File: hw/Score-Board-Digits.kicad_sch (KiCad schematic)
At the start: 65 parts, among them J11 Conn_02x09_Odd_Even, J12 Conn_02x09_Odd_Even, J13 Conn_02x09_Odd_Even

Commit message: Separate Main and Digits projects
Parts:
- DIG1, DIG2: footprint Display_7Segment:SA15-11xxx -> AES_Library:DISP-40101BCR-AES
- DIG5, DIG6: footprint Display_7Segment:SA15-11xxx -> AES_Library:DISP-CL18011BS-AES
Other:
- title: Portable Score Board w/Remote -> Portable Score Board - Digits

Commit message: Digits schmatic ready for layout
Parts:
- removed DIG1, DIG2: WJLEDS40012TUR11, AES_Library:DISP-40101BCR-AES, symbol AES_Library:WJ-LEDS40012TUR11
- removed DIG5 (x3), DIG6: WJLEDS18012TUR11, AES_Library:DISP-CL18011BS-AES, symbol AES_Library:WJ-LEDS18012TUR11
- removed H1 (x2), H2 (x2), H3 (x2), H4 (x2): MountingHole, MountingHole:MountingHole_3.2mm_M3, symbol Mechanical:MountingHole
- removed J12, J13: Conn_02x09_Odd_Even, Connector_PinHeader_2.54mm:PinHeader_2x09_P2.54mm_Vertical, symbol Connector_Generic:Conn_02x09_Odd_Even
- removed LED4: IND-B1, LED_THT:LED_D5.0mm-3, symbol Device:LED
- removed LED5: IND-B2, LED_THT:LED_D5.0mm-3, symbol Device:LED
- removed LED6: IND-B3, LED_THT:LED_D5.0mm-3, symbol Device:LED
- removed LED7: IND-B4, LED_THT:LED_D5.0mm-3, symbol Device:LED
- removed R25, R26, R27, R28, R29, R30, R31: 150, Resistor_THT:R_Axial_DIN0207_L6.3mm_D2.5mm_P10.16mm_Horizontal, symbol Device:R_Small_US
- removed R25, R26, R27, R28, R29, R30, R31, R32 (x2): 0, Resistor_THT:R_Axial_DIN0207_L6.3mm_D2.5mm_P10.16mm_Horizontal, symbol Device:R_Small_US
- added Opt1, Opt2, Opt3, Opt4, Opt5: Opt_1-2, Connector_PinHeader_2.54mm:PinHeader_1x03_P2.54mm_Vertical, symbol AES_Library:Opt_1_of_2
- DIG1: renamed from DIG5; footprint AES_Library:DISP-CL18011BS-AES -> Connector_PinHeader_2.54mm:PinHeader_1x03_P2.54mm_Vertical
- renumbered DIG5 to DIG2, DIG1 to DIG3, DIG2 to DIG4, J11 to J1, LED4 to LED1, LED5 to LED2, LED6 to LED3, LED7 to LED4, R25 to R1, R22 to R10, R23 to R11, R24 to R12, R21 to R13, R22 to R14, R23 to R15, R24 to R16, R26 to R2, R27 to R3, R28 to R4, R29 to R5, R30 to R6, R31 to R7, R32 to R8, R21 to R9
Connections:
- net SD.B.E is gone; now on net SD.E: R13.1
- net SD.B.F is gone; now on net SD.F: R14.1
- net SD.B.G is gone; now on net SD.G: R15.1
- net SD.B.P is gone; now on net SD.P: R16.1
- net at DIG2.1 (CA), DIG2.5 (CA), DIG4.1 (CA)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: now also Opt3.2 (Pin_Common), Opt4.2 (Pin_Common); no longer J1.4 (Pin_4)
- net at R13.2: now also LED1.1 (K), R9.2
- net at R16.2: now also LED4.1 (K), R12.2
- net at LED3.1 (K), R11.2: now also R15.2
- net at DIG1.1 (CA), DIG1.5 (CA), DIG3.1 (CA)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: now also Opt1.2 (Pin_Common), Opt2.2 (Pin_Common); no longer J1.2 (Pin_2)
- net at R14.2: now also LED2.1 (K), R10.2
- net at LED1.2 (A), LED2.2 (A), LED3.2 (A)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: now also Opt5.2 (Pin_Common); no longer J1.14 (Pin_14)
- net at J1.10 (Pin_10): now also Opt2.1 (Pin_A)
- net at J1.12 (Pin_12): now also Opt4.1 (Pin_A)
- net at J1.16 (Pin_16): now also Opt5.3 (Pin_B)
- net at J1.6 (Pin_6): now also Opt1.3 (Pin_B)
- net at J1.8 (Pin_8): now also Opt3.3 (Pin_B)
- net SD.A.A renamed SD.A
- net SD.A.B renamed SD.B
- net SD.A.C renamed SD.C
- net SD.A.D renamed SD.D
- net SD.A.E renamed SD.E
- net SD.A.F renamed SD.F
- net SD.A.G renamed SD.G
- net SD.A.P renamed SD.P
- new net: J1.4 (Pin_4), Opt3.1 (Pin_A)
- new net: J1.2 (Pin_2), Opt1.1 (Pin_A)
- new net: J1.14 (Pin_14), Opt5.1 (Pin_A)
- no-connect marks 16 -> 2
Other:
- note added: "(LARGE DIGIT ASSY)"
- note added: "(SMALL DIGIT ASSY)"
- note added: "Indicators A/B/None Populate Resistors for A-D or E-P and select Option A or B"
- note removed: "(LARGE DIGIT OPTION)"
- note removed: "(SMALLER DIGIT OPTION)"
- note removed: "PERIOD / TIME (BOARD C)"
- note removed: "TEAM A SCORE & INDICATORS (BOARD A)"
- note removed: "TEAM B SCORE & INDICATORS (BOARD B)"
- moved on the sheet: DIG1, DIG2, DIG3, DIG4, H1, H2, H3, H4, J1, LED1, LED2, LED3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

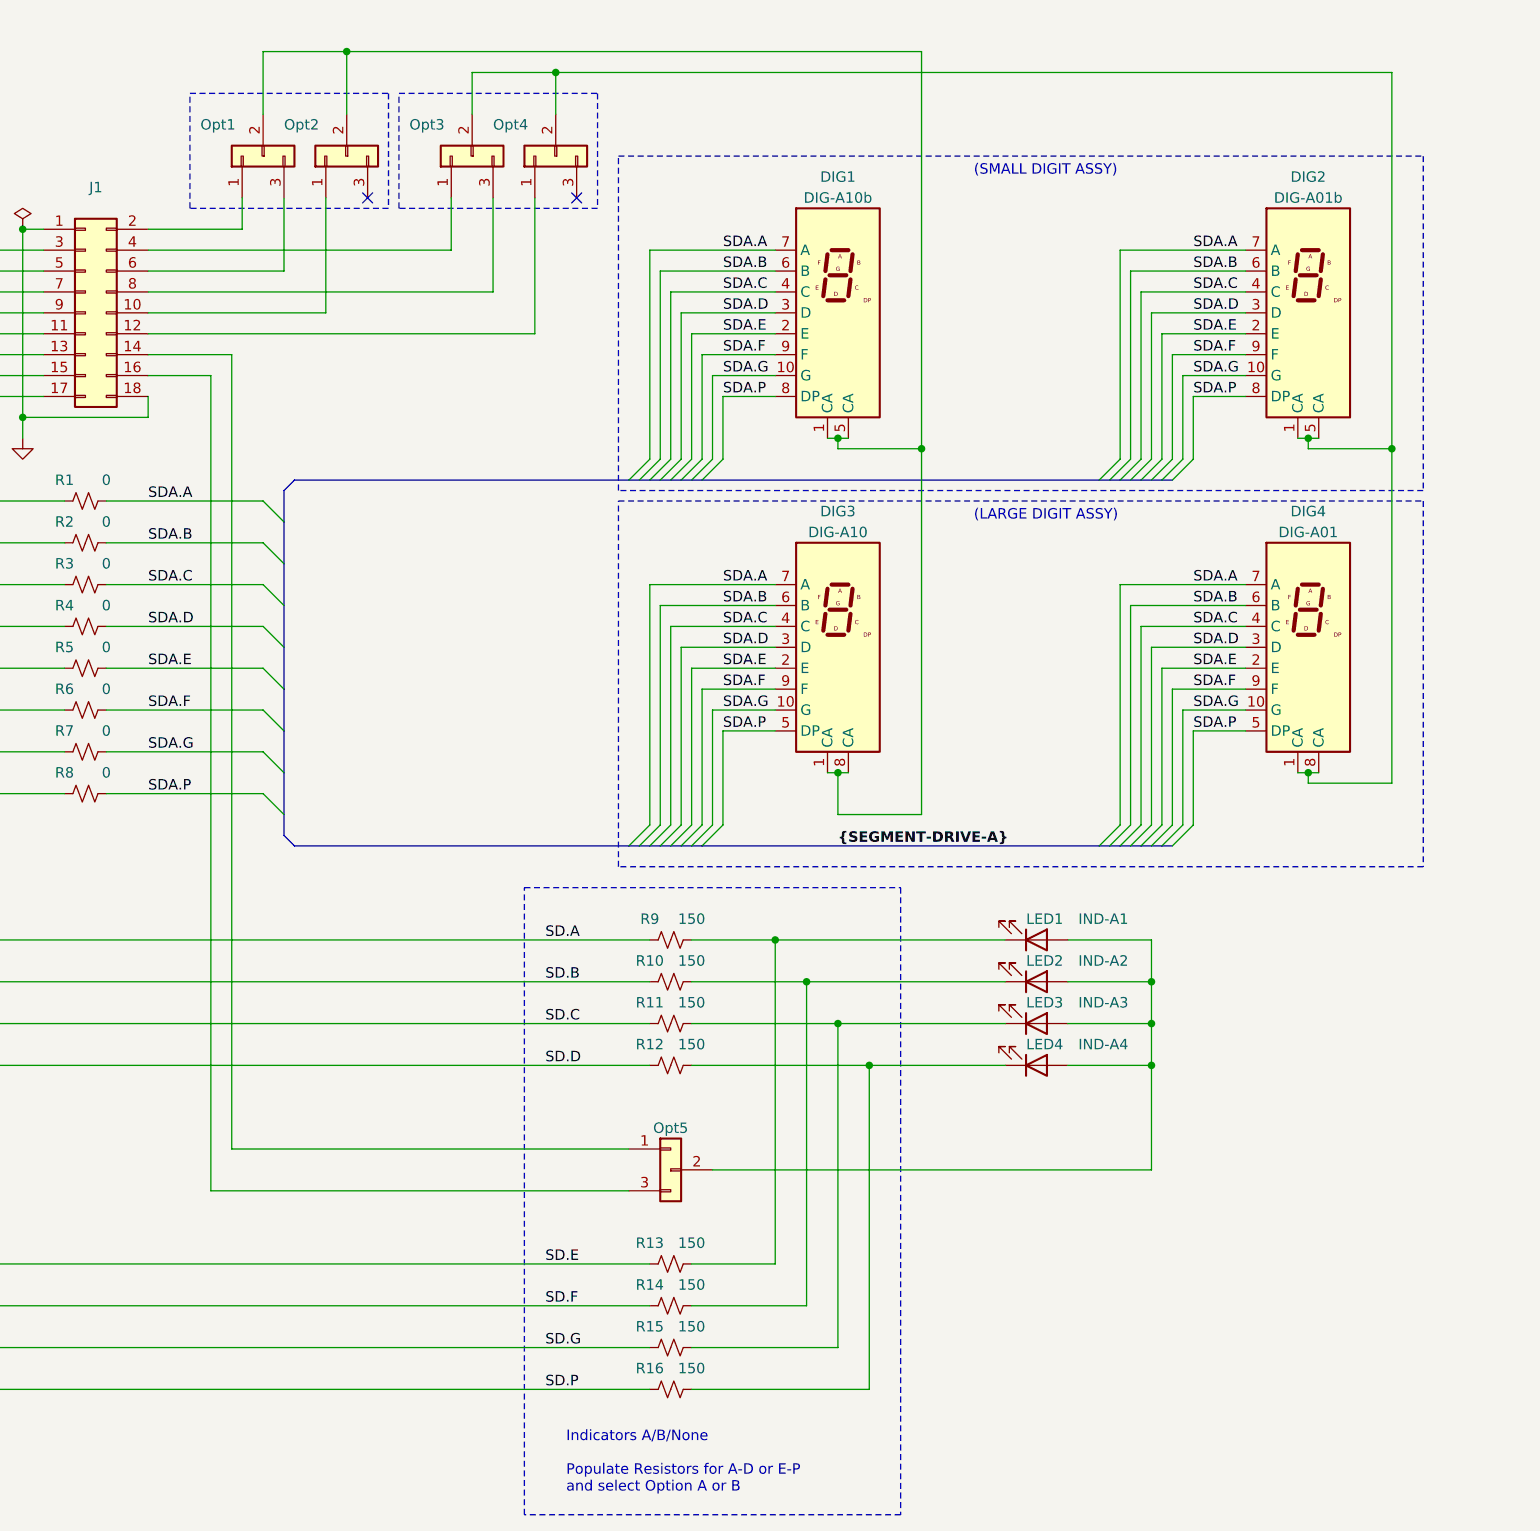
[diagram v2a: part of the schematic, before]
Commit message: Initial PCB component placement
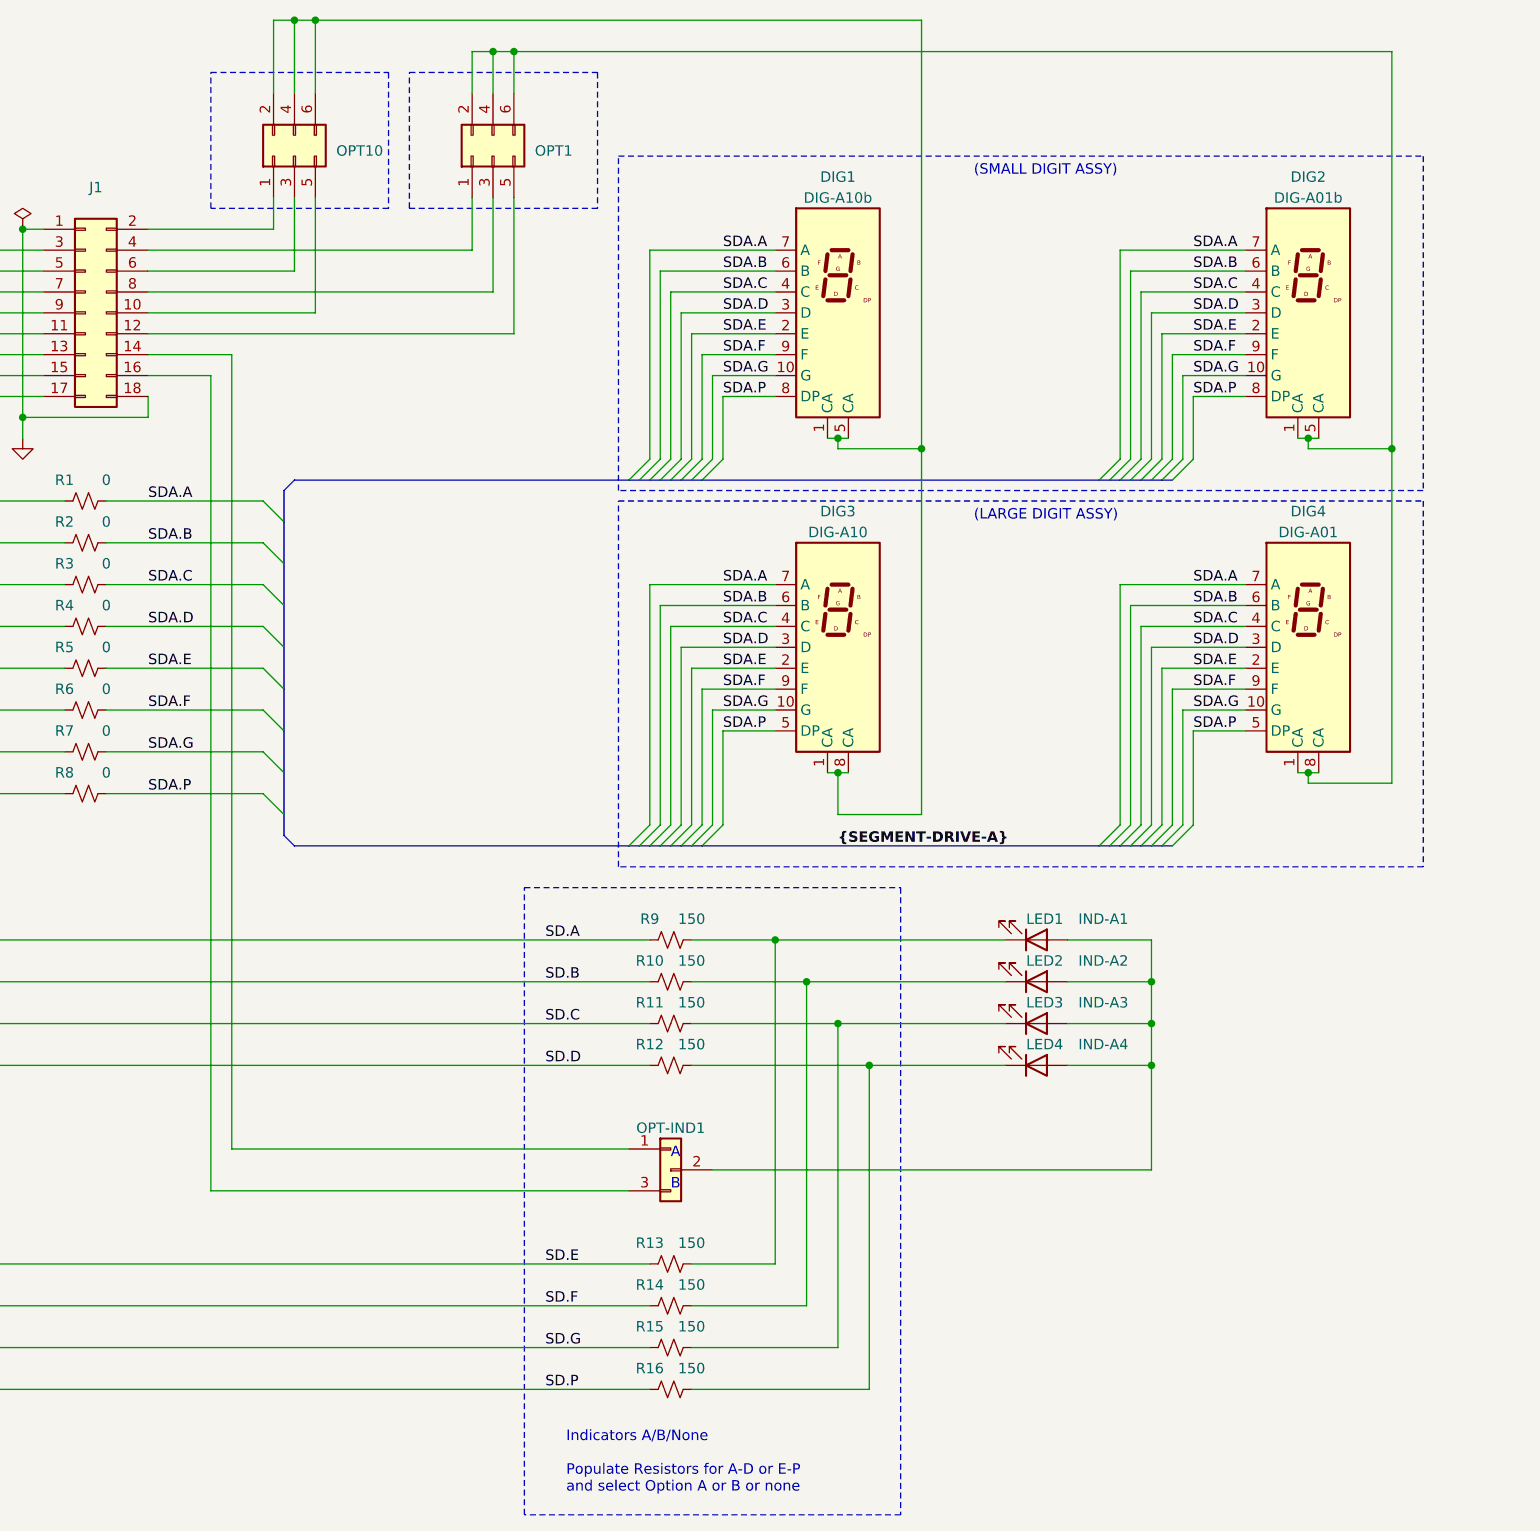
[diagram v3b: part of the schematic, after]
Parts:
- removed Opt1, Opt2, Opt3, Opt4: Opt_1-2, Connector_PinHeader_2.54mm:PinHeader_1x03_P2.54mm_Vertical, symbol AES_Library:Opt_1_of_2
- added OPT1, OPT10: Conn_02x03_Odd_Even, Connector_PinHeader_2.54mm:PinHeader_2x03_P2.54mm_Vertical, symbol Connector_Generic:Conn_02x03_Odd_Even
- DIG1: footprint Connector_PinHeader_2.54mm:PinHeader_1x03_P2.54mm_Vertical -> AES_Library:DISP-CL18011BS-AES
- LED1, LED2, LED3, LED4: footprint LED_THT:LED_D5.0mm-3 -> LED_THT:LED_D5.0mm
- renumbered Opt5 to OPT-IND1
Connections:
- net at J1.4 (Pin_4): now also OPT1.1 (Pin_1)
- net at DIG2.1 (CA), DIG2.5 (CA), DIG4.1 (CA)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: now also OPT1.2 (Pin_2), OPT1.4 (Pin_4), OPT1.6 (Pin_6)
- net at J1.8 (Pin_8): now also OPT1.3 (Pin_3)
- net at J1.2 (Pin_2): now also OPT10.1 (Pin_1)
- net at DIG1.1 (CA), DIG1.5 (CA), DIG3.1 (CA)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: now also OPT10.2 (Pin_2), OPT10.4 (Pin_4), OPT10.6 (Pin_6)
- net at J1.6 (Pin_6): now also OPT10.3 (Pin_3)
- net at J1.12 (Pin_12): now also OPT1.5 (Pin_5)
- net at J1.10 (Pin_10): now also OPT10.5 (Pin_5)
- no-connect marks 2 -> 0
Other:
- note added: "A"
- note added: "B"
- note added: "Indicators A/B/None Populate Resistors for A-D or E-P and select Option A or B or none"
- note removed: "Indicators A/B/None Populate Resistors for A-D or E-P and select Option A or B"

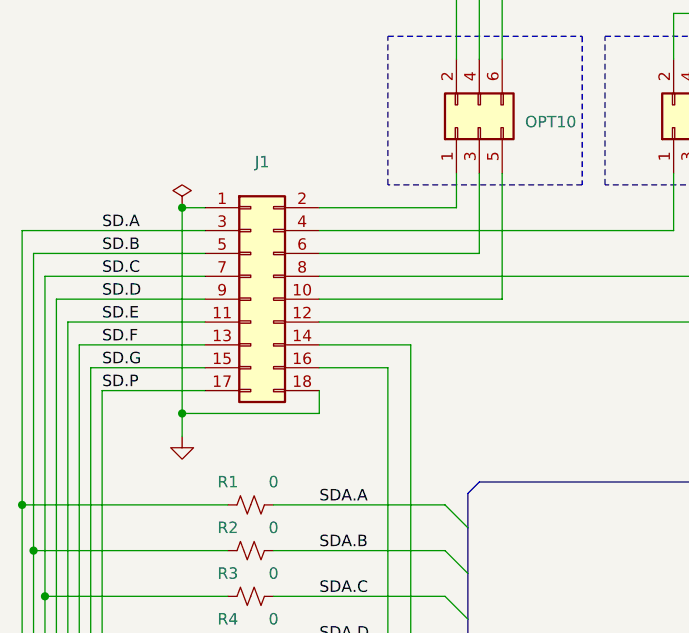
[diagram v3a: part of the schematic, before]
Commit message: Main schematic ready for board layout
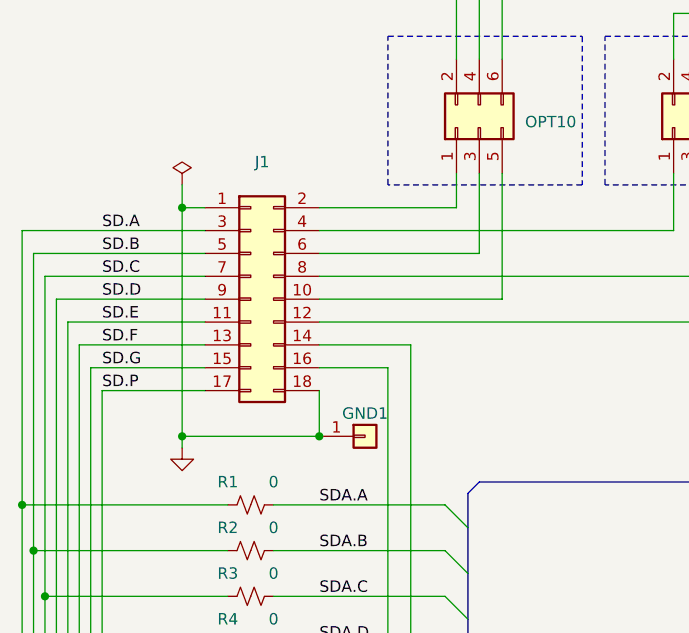
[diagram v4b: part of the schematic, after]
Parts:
- added GND1: Conn_01x01, Connector_PinHeader_2.54mm:PinHeader_1x01_P2.54mm_Vertical, symbol Connector_Generic:Conn_01x01
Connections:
- net GND: now also GND1.1 (Pin_1)
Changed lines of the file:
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@@
   (junction (at 20.32 74.93) (diameter 0) (color 0 0 0 0)
   )
+  (junction (at 38.1 67.31) (diameter 0) (color 0 0 0 0)
+  )
   (junction (at 175.26 138.43) (diameter 0) (color 0 0 0 0)
   )
@@
   (junction (at 29.21 110.49) (diameter 0) (color 0 0 0 0)
   )
+  (junction (at 53.34 67.31) (diameter 0) (color 0 0 0 0)
+  )
   (junction (at 147.32 68.58) (diameter 0) (color 0 0 0 0)
   )
@@
   (junction (at 137.16 107.95) (diameter 0) (color 0 0 0 0)
   )
-  (junction (at 38.1 64.77) (diameter 0) (color 0 0 0 0)
-  )
   (junction (at 194.31 107.95) (diameter 0) (color 0 0 0 0)
   )
@@
     (stroke (width 0) (type default))
   )
-  (wire (pts (xy 53.34 64.77) (xy 38.1 64.77))
+  (wire (pts (xy 53.34 67.31) (xy 38.1 67.31))
     (stroke (width 0) (type default))
   )
@@
     (stroke (width 0) (type default))
   )
+  (wire (pts (xy 53.34 62.23) (xy 53.34 67.31))
+    (stroke (width 0) (type default))
+  )
   (bus (pts (xy 115.57 116.84) (xy 116.84 116.84))
     (stroke (width 0) (type default))
@@
     (stroke (width 0) (type default))
   )
+  (wire (pts (xy 38.1 41.91) (xy 38.1 67.31))
+    (stroke (width 0) (type default))
+  )
   (bus (pts (xy 120.65 116.84) (xy 168.91 116.84))
     (stroke (width 0) (type default))
@@
     (stroke (width 0) (type default))
   )
-  (wire (pts (xy 53.34 62.23) (xy 53.34 64.77))
-    (stroke (width 0) (type default))
-  )
   (wire (pts (xy 137.16 177.8) (xy 137.16 138.43))
     (stroke (width 0) (type default))
@@
     (stroke (width 0) (type default))
   )
-  (wire (pts (xy 38.1 41.91) (xy 38.1 64.77))
-    (stroke (width 0) (type default))
-  )
   (wire (pts (xy 48.26 110.49) (xy 67.31 110.49))
     (stroke (width 0) (type default))
@@
     (stroke (width 0) (type default))
   )
+  (wire (pts (xy 38.1 39.37) (xy 38.1 41.91))
+    (stroke (width 0) (type default))
+  )
   (wire (pts (xy 68.58 16.51) (xy 68.58 25.4))
     (stroke (width 0) (type default))
@@
     (stroke (width 0) (type default))
   )
+  (wire (pts (xy 38.1 67.31) (xy 38.1 68.58))
+    (stroke (width 0) (type default))
+  )
   (wire (pts (xy 194.31 107.95) (xy 195.58 107.95))
     (stroke (width 0) (type default))
@@
   )
   (bus (pts (xy 172.72 116.84) (xy 173.99 116.84))
-    (stroke (width 0) (type default))
-  )
-  (wire (pts (xy 38.1 64.77) (xy 38.1 67.31))
     (stroke (width 0) (type default))
   )
@@
     (effects (font (size 1.27 1.27)) (justify left bottom))
   )
-  (netclass_flag "" (length 2.54) (shape round) (at 38.1 67.31 270)
+  (netclass_flag "" (length 2.54) (shape round) (at 38.1 39.37 270)
     (effects (font (size 1.27 1.27)) (justify right bottom))
-    (property "Netclass" "GND" (at 41.91 67.31 0)
-      (effects (font (size 1.27 1.27) italic) (justify left))
+    (property "Netclass" "GND" (at 41.91 39.37 0)
+      (effects (font (size 1.27 1.27) italic) (justify left) hide)
     )
   )
@@
     )
   )
-  (symbol (lib_id "power:PWR_FLAG") (at 38.1 41.91 0) (unit 1)
+  (symbol (lib_id "power:PWR_FLAG") (at 38.1 39.37 0) (unit 1)
     (in_bom yes) (on_board yes) (dnp no) (fields_autoplaced)
-    (property "Reference" "#FLG01" (at 38.1 40.005 0)
-      (effects (font (size 1.27 1.27)) hide)
-    )
-    (property "Value" "PWR_FLAG" (at 38.1 38.1 0)
-      (effects (font (size 1.27 1.27)) hide)
-    )
-    (property "Footprint" "" (at 38.1 41.91 0)
-      (effects (font (size 1.27 1.27)) hide)
-    )
-    (property "Datasheet" "~" (at 38.1 41.91 0)
+    (property "Reference" "#FLG01" (at 38.1 37.465 0)
+      (effects (font (size 1.27 1.27)) hide)
+    )
+    (property "Value" "PWR_FLAG" (at 38.1 35.56 0)
+      (effects (font (size 1.27 1.27)) hide)
+    )
+    (property "Footprint" "" (at 38.1 39.37 0)
+      (effects (font (size 1.27 1.27)) hide)
+    )
+    (property "Datasheet" "~" (at 38.1 39.37 0)
       (effects (font (size 1.27 1.27)) hide)
     )
@@
     )
   )
+  (symbol (lib_id "Connector_Generic:Conn_01x01") (at 58.42 67.31 0) (unit 1)
+    (in_bom yes) (on_board yes) (dnp no)
+    (property "Reference" "GND1" (at 55.88 64.77 0)
+      (effects (font (size 1.27 1.27)) (justify left))
+    )
+    (property "Value" "Conn_01x01" (at 60.96 69.215 0)
+      (effects (font (size 1.27 1.27)) (justify left) hide)
+    )
+    (property "Footprint" "Connector_PinHeader_2.54mm:PinHeader_1x01_P2.54mm_Vertical" (at 58.42 67.31 0)
+      (effects (font (size 1.27 1.27)) hide)
+    )
+    (property "Datasheet" "~" (at 58.42 67.31 0)
+      (effects (font (size 1.27 1.27)) hide)
+    )
+    (pin "1")
+    (instances
+      (project "Score-Board-Digits"
+        (path "/6837b59f-09d9-4828-b818-e554889c44cd"
+          (reference "GND1") (unit 1)
+        )
+      )
+    )
+  )
   (symbol (lib_id "AES_Library:Opt_1_of_2") (at 116.84 156.21 0) (unit 1)
     (in_bom yes) (on_board yes) (dnp no) (fields_autoplaced)
@@
     )
   )
-  (symbol (lib_id "power:GND") (at 38.1 67.31 0) (unit 1)
+  (symbol (lib_id "power:GND") (at 38.1 68.58 0) (unit 1)
     (in_bom yes) (on_board yes) (dnp no) (fields_autoplaced)
-    (property "Reference" "#PWR01" (at 38.1 73.66 0)
-      (effects (font (size 1.27 1.27)) hide)
-    )
-    (property "Value" "GND" (at 38.1 72.39 0)
-      (effects (font (size 1.27 1.27)) hide)
-    )
-    (property "Footprint" "" (at 38.1 67.31 0)
-      (effects (font (size 1.27 1.27)) hide)
-    )
-    (property "Datasheet" "" (at 38.1 67.31 0)
-      (effects (font (size 1.27 1.27)) hide)
-    )
+    (property "Reference" "#PWR01" (at 38.1 74.93 0)
+      (effects (font (size 1.27 1.27)) hide)
+    )
+    (property "Value" "GND" (at 38.1 73.66 0)
+      (effects (font (size 1.27 1.27)) hide)
+    )
+    (property "Footprint" "" (at 38.1 68.58 0)
+      (effects (font (size 1.27 1.27)) hide)
+    )
+    (property "Datasheet" "" (at 38.1 68.58 0)
+      (effects (font (size 1.27 1.27)) hide)
+    )
